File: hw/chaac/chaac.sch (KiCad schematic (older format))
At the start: 58 parts, among them J1 windrain, J2 chaac_radio, J3 chaac_radio, J4 AM2315, J5 Battery, J6 Solar Panel, J7 UART, Q1 Q_PMOS_GSD, SW1 RST, SW2 RST, U1 MIC550X, U2 BMP280, U3 MCP73871

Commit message: Released chaac v3.1 to OSHPark
Moved NRF52 back into chaac pcb.
Removed external T/H connector, switched to BME280 for temp, humidity,
and pressure sensing.

Using RP-SMA connector for this version.
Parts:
- removed J2, J3: chaac_radio, alvarop:20021121-00016C4LF, symbol Connector_Generic:Conn_02x08_Odd_Even
- removed J4: AM2315, TerminalBlock_TE-Connectivity:TerminalBlock_TE_282834-4_1x04_P2.54mm_Horizontal, symbol Connector_Generic:Conn_01x04
- removed U2: BMP280, alvarop:BMP280, symbol alvarop:BMP280
- added C10, C17, C9: 0.1uF, Capacitor_SMD:C_0402_1005Metric, symbol Device:C_Small
- added C11, C12, C13, C15: 12pF, Capacitor_SMD:C_0402_1005Metric, symbol Device:C_Small
- added C14: 100pF, Capacitor_SMD:C_0402_1005Metric, symbol Device:C_Small
- added C16: DNP, Capacitor_SMD:C_0402_1005Metric, symbol Device:C_Small
- added C7: 1uF, Capacitor_SMD:C_0402_1005Metric, symbol Device:C_Small
- added C8: 4.7uF, Capacitor_SMD:C_0402_1005Metric, symbol Device:C_Small
- added F1: 2450FM07A0029T, alvarop:2450FM07A0029T, symbol alvarop:2450FM07A0029T
- added J3: Conn_Coaxial, Connector_Coaxial:SMA_Samtec_SMA-J-P-H-ST-EM1_EdgeMount, symbol Connector:Conn_Coaxial
- added J4: TC2030-CTX, alvarop:TC2030-NL, symbol alvarop:TC2030-CTX
- added L1: 15nH, Inductor_SMD:L_0402_1005Metric, symbol Device:L_Small
- added L2: 10uH, Inductor_SMD:L_0603_1608Metric, symbol Device:L_Small
- added U3: NRF52811-QFAA, alvarop:NRF52811-QFN48, symbol alvarop:NRF52811-QFAA
- added U4: BME280, alvarop:BME280, symbol alvarop:BME280
- added Y1: 32MHz, Crystal:Crystal_SMD_2016-4Pin_2.0x1.6mm, symbol Device:Crystal_GND24
- added Y2: 32.768kHz, Crystal:Crystal_SMD_3215-2Pin_3.2x1.5mm, symbol Device:Crystal_Small
- R3: renamed from R19; value 2k -> 33k; DKPN CR0603-FX-2001ELFCT-ND -> 311-33.0KHRCT-ND; MPN CR0603-FX-2001ELF -> RC0603FR-0733KL
- renumbered C11 to C1, C8 to C18, C2 to C19, C12 to C2, C4 to C20, C7 to C21, C10 to C22, C5 to C23, C3 to C24, C9 to C25, C1 to C3, C6 to C4, C14 to C5, C13 to C6, D3 to D1, D4 to D2, D5 to D3, D6 to D4, D1 to D5, D2 to D6, J6 to J1, J5 to J2, J1 to J5, J7 to J6, R21 to R1, R9 to R10, R12 to R11, R10 to R12, R1 to R14, R2 to R15, R3 to R18, R4 to R19, R22 to R2, R11 to R20, R7 to R21, R14 to R22, R15 to R23, R5 to R24, R6 to R25, R20 to R4, R23 to R5, R18 to R6, R24 to R7, R25 to R8, R8 to R9, U3 to U2
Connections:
- net labels added: ANT, RF_OUT, SWDCLK, SWDIO
- wire segments 243 -> 323
- no-connect marks 23 -> 24
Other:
- note added: "1000V/(33k)=30mA"
- note removed: "1000V/(2k)=500mA"
- note removed: "7-bit I2C Addr: 0x5C"
- moved on the sheet: C1, C18, C19, C2, C20, C21, C22, C23, C24, C25, C3, C4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

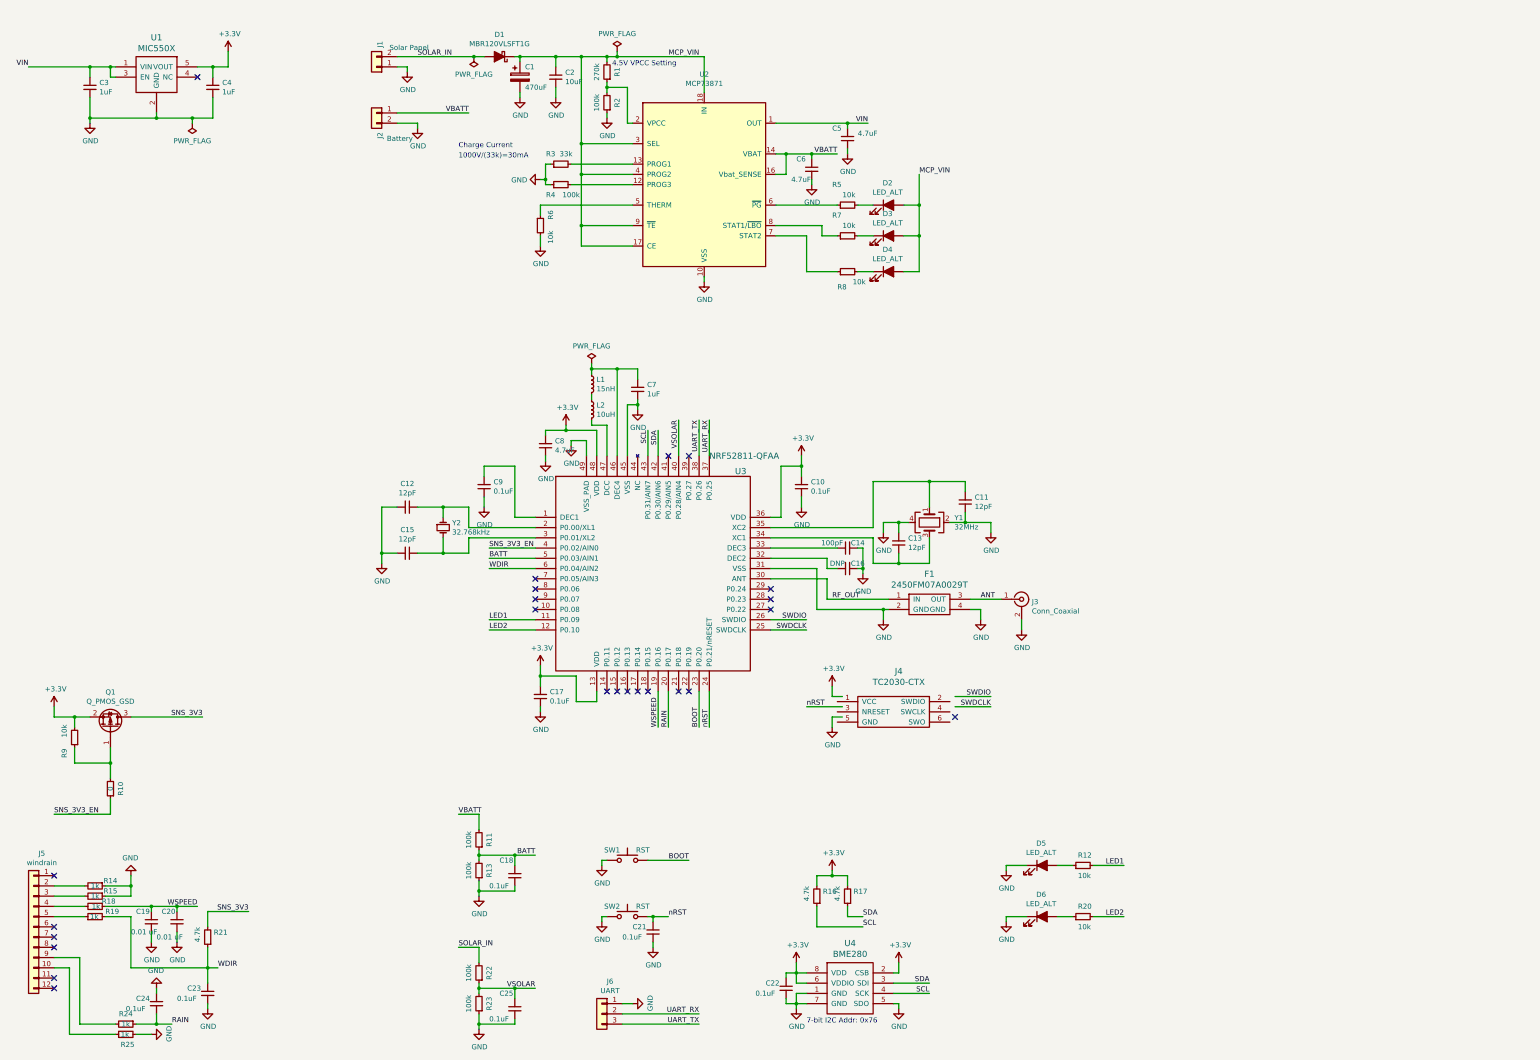
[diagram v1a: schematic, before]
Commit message: Started chaac v4.0 Schematic + layout
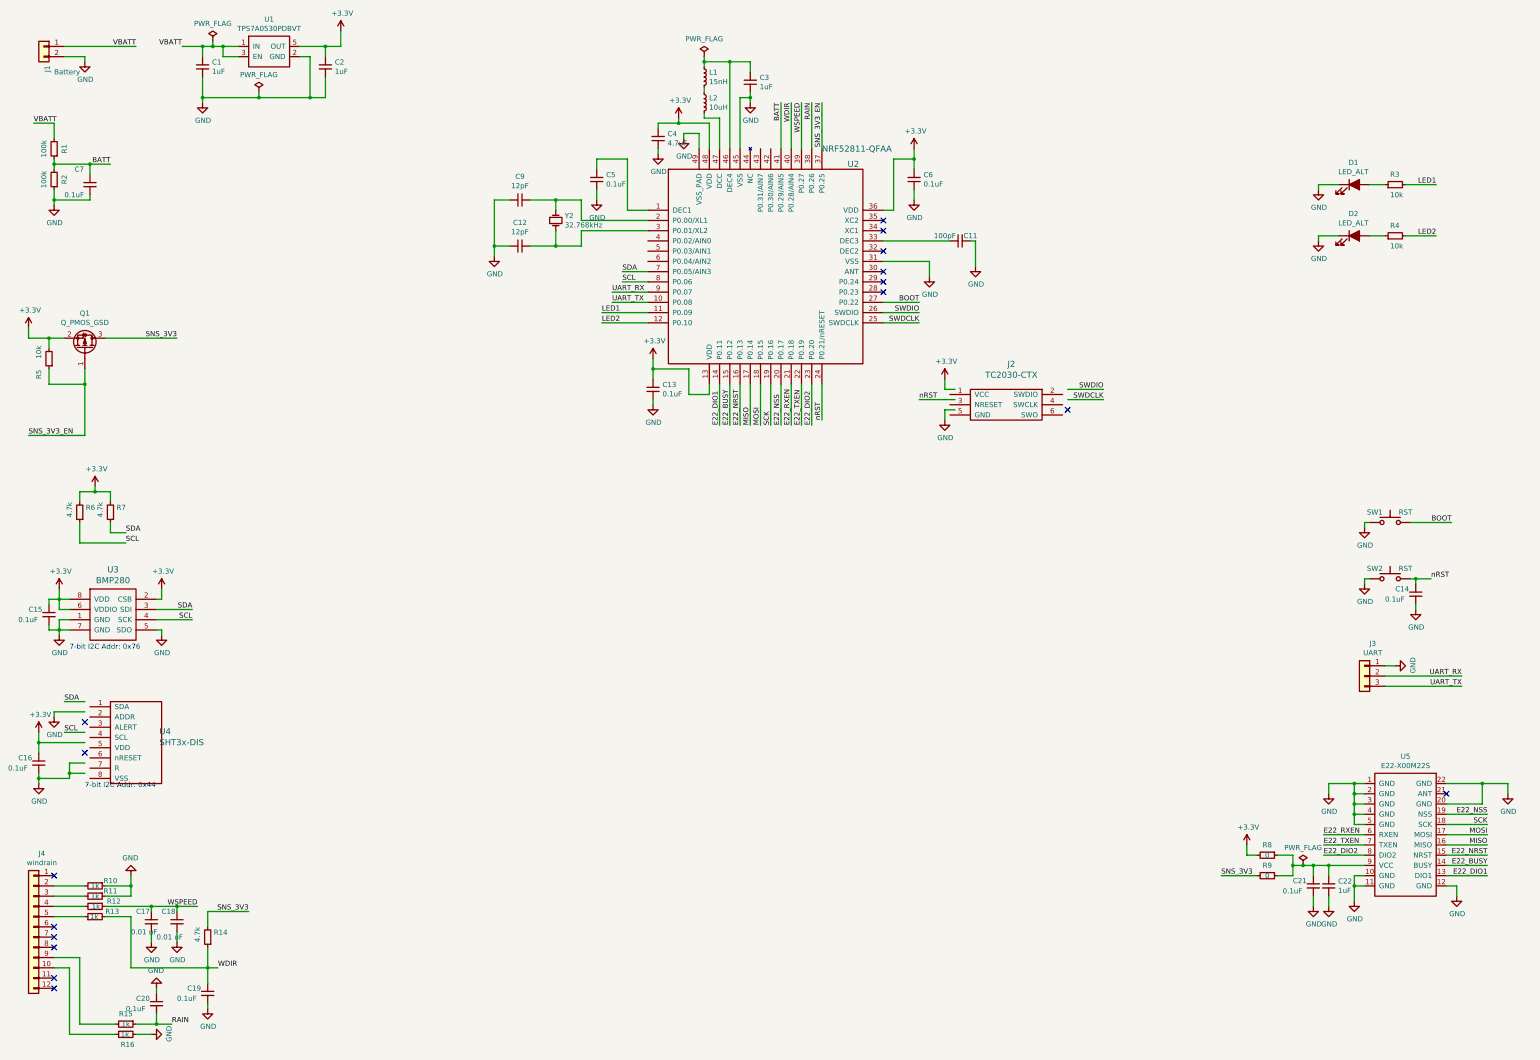
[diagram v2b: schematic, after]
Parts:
- removed C1: 470uF, Capacitor_SMD:CP_Elec_8x10, symbol Device:CP
- removed C11, C13: 12pF, Capacitor_SMD:C_0402_1005Metric, symbol Device:C_Small
- removed C2: 10uF, Capacitor_SMD:C_0805_2012Metric, symbol Device:C_Small
- removed C25: 0.1uF, Capacitor_SMD:C_0603_1608Metric, symbol Device:C_Small
- removed C5, C6: 4.7uF, Capacitor_SMD:C_0603_1608Metric, symbol Device:C_Small
- removed D1: MBR120VLSFT1G, Diode_SMD:D_SOD-123F, symbol Device:D_Schottky_ALT
- removed D2, D3, D4: LED_ALT, LED_SMD:LED_0603_1608Metric, symbol Device:LED_ALT
- removed F1: 2450FM07A0029T, alvarop:2450FM07A0029T, symbol alvarop:2450FM07A0029T
- removed J1: Solar Panel, TerminalBlock_TE-Connectivity:TerminalBlock_TE_282834-2_1x02_P2.54mm_Horizontal, symbol Connector_Generic:Conn_01x02
- removed J3: Conn_Coaxial, Connector_Coaxial:SMA_Samtec_SMA-J-P-H-ST-EM1_EdgeMount, symbol Connector:Conn_Coaxial
- removed R1: 270k, Resistor_SMD:R_0603_1608Metric, symbol Device:R_Small
- removed R10: 0, Resistor_SMD:R_0603_1608Metric, symbol Device:R_Small
- removed R2, R22, R23, R4: 100k, Resistor_SMD:R_0603_1608Metric, symbol Device:R_Small
- removed R3: 33k, Resistor_SMD:R_0603_1608Metric, symbol Device:R_Small
- removed R5, R6, R7: 10k, Resistor_SMD:R_0603_1608Metric, symbol Device:R_Small
- removed U1: MIC550X, alvarop:SOT-23(M5), symbol alvarop:MIC550X
- removed U2: MCP73871, alvarop:MCP73871, symbol Battery_Management:MCP73871
- removed U4: BME280, alvarop:BME280, symbol alvarop:BME280
- removed Y1: 32MHz, Crystal:Crystal_SMD_2016-4Pin_2.0x1.6mm, symbol Device:Crystal_GND24
- added C21: 0.1uF, Capacitor_SMD:C_0603_1608Metric, symbol Device:C_Small
- added C22: 1uF, Capacitor_SMD:C_0603_1608Metric, symbol Device:C_Small
- added R9: 0, Resistor_SMD:R_0603_1608Metric, symbol Device:R_Small
- added U1: TPS7A0530PDBVT, alvarop:SOT-23(M5), symbol alvarop:TPS7A0530PDBVT
- added U3: BMP280, alvarop:BMP280, symbol alvarop:BMP280
- added U4: SHT3x-DIS, alvarop:SHT3x, symbol alvarop:SHT3x-DIS
- added U5: E22-X00M22S, alvarop:E22-X00M22S, symbol alvarop:E22-X00M22S
- C16: value DNP -> 0.1uF; footprint Capacitor_SMD:C_0402_1005Metric -> Capacitor_SMD:C_0603_1608Metric; DKPN (none) -> 490-1532-1-ND; MPN (none) -> GRM188R71C104KA01D
- J1: renamed from J2; footprint alvarop:S2B-PH-SM4-TB -> alvarop:‎282837-2‎
- R8: value 10k -> 0; DKPN 311-10.0KHRCT-ND -> (none); MPN RC0603FR-0710KL -> (none)
- renumbered C3 to C1, C14 to C11, C15 to C12, C17 to C13, C21 to C14, C22 to C15, C19 to C17, C20 to C18, C23 to C19, C4 to C2, C24 to C20, C7 to C3, C8 to C4, C9 to C5, C10 to C6, C18 to C7, C12 to C9, D5 to D1, D6 to D2, J4 to J2, J6 to J3, J5 to J4, R11 to R1, R14 to R10, R15 to R11, R18 to R12, R19 to R13, R21 to R14, R24 to R15, R25 to R16, R13 to R2, R12 to R3, R20 to R4, R9 to R5, R16 to R6, R17 to R7, U3 to U2
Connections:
- net labels added: E22_BUSY, E22_DIO1, E22_DIO2, E22_NRST, E22_NSS, E22_RXEN, E22_TXEN, MISO, MOSI, SCK
- net labels removed: ANT, MCP_VIN, RF_OUT, SOLAR_IN, VIN, VSOLAR
- wire segments 323 -> 280
- no-connect marks 24 -> 16
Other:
- note added: "7-bit I2C Addr: 0x44"
- note removed: "1000V/(33k)=30mA"
- note removed: "4.5V VPCC Setting"
- note removed: "Charge Current"
- moved on the sheet: C1, C11, C12, C13, C14, C15, C2, C3, C4, C5, C6, C7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

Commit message: Finished chaac v4.0!
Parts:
- J1: footprint alvarop:‎282837-2‎ -> TerminalBlock_TE-Connectivity:TerminalBlock_TE_282834-2_1x02_P2.54mm_Horizontal
- U2: footprint alvarop:NRF52811-QFN48 -> alvarop:NRF52811-QFN48-VIAS
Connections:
- no-connect marks 16 -> 21
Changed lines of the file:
@@
 Sheet 1 1
 Title "Chaac"
-Date "2020-06-15"
+Date "2020-06-16"
 Rev "4.0"
 Comp "@alvaroprieto"
@@
 L Connector_Generic:Conn_01x02 J1
 U 1 1 5D0543CF
-P 1350 1100
-F 0 "J1" V 1316 912 50  0000 R CNN
-F 1 "Battery" H 1250 850 50  0000 R CNN
-F 2 "alvarop:‎282837-2‎" H 1350 1100 50  0001 C CNN
-F 3 "~" H 1350 1100 50  0001 C CNN
-F 4 "S2B-PH-SM4-TB(LF)(SN)" V 1350 1100 50  0001 C CNN "MPN"
-F 5 "455-1749-1-ND" V 1350 1100 50  0001 C CNN "DKPN"
-	1    1350 1100
-	-1   0    0    -1
+P 1350 1200
+F 0 "J1" V 1316 1012 50  0000 R CNN
+F 1 "Battery" H 1250 950 50  0000 R CNN
+F 2 "TerminalBlock_TE-Connectivity:TerminalBlock_TE_282834-2_1x02_P2.54mm_Horizontal" H 1350 1200 50  0001 C CNN
+F 3 "~" H 1350 1200 50  0001 C CNN
+F 4 "S2B-PH-SM4-TB(LF)(SN)" V 1350 1200 50  0001 C CNN "MPN"
+F 5 "455-1749-1-ND" V 1350 1200 50  0001 C CNN "DKPN"
+	1    1350 1200
+	-1   0    0    1
 $EndComp
 Wire Wire Line
@@
 U 1 1 5D925286
 P 7350 2000
-F 0 "C4" H 7258 1954 50  0000 R CNN
-F 1 "4.7uF" H 7258 2045 50  0000 R CNN
+F 0 "C4" H 7550 1950 50  0000 R CNN
+F 1 "4.7uF" H 7600 2100 50  0000 R CNN
 F 2 "Capacitor_SMD:C_0402_1005Metric" H 7350 2000 50  0001 C CNN
 F 3 "~" H 7350 2000 50  0001 C CNN
@@
 Connection ~ 7800 1250
 Wire Wire Line
-	7250 3700 6800 3700
-Text Label 6800 3700 0    50   ~ 0
+	7250 3300 6800 3300
+Text Label 6800 3400 0    50   ~ 0
 LED1
 Wire Wire Line
-	7250 3800 6800 3800
-Text Label 6800 3800 0    50   ~ 0
+	7250 3400 6800 3400
+Text Label 6800 3300 0    50   ~ 0
 LED2
 Wire Wire Line
 	7250 3500 6900 3500
-Text Label 6900 3500 0    50   ~ 0
+Text Label 6900 3700 0    50   ~ 0
 UART_RX
-Text Label 6900 3600 0    50   ~ 0
+Text Label 6900 3800 0    50   ~ 0
 UART_TX
 Wire Wire Line
@@
 F 0 "U2" H 9200 4250 60  0000 L CNN
 F 1 "NRF52811-QFAA" H 8950 4400 60  0000 L CNN
-F 2 "alvarop:NRF52811-QFN48" H 7250 3800 50  0001 C CNN
+F 2 "alvarop:NRF52811-QFN48-VIAS" H 7250 3800 50  0001 C CNN
 F 3 "" H 7250 3800 50  0001 C CNN
 F 4 "‎1490-1075-1-ND‎" H 8400 3250 50  0001 C CNN "DKPN"
@@
 	1    0    0    -1
 $EndComp
-Wire Wire Line
-	8150 4800 8150 4400
-Wire Wire Line
-	8050 4800 8050 4400
-Wire Wire Line
-	7950 4800 7950 4400
-Wire Wire Line
-	8450 4800 8450 4400
-Wire Wire Line
-	8350 4800 8350 4400
-Wire Wire Line
-	8250 4800 8250 4400
-Wire Wire Line
-	8550 4400 8550 4800
-Text Label 8550 4800 1    50   ~ 0
-E22_NSS
-Text Label 8450 4800 1    50   ~ 0
-SCK
-Text Label 8350 4800 1    50   ~ 0
-MOSI
-Text Label 8250 4800 1    50   ~ 0
-MISO
-Text Label 8150 4800 1    50   ~ 0
-E22_NRST
-Text Label 8050 4800 1    50   ~ 0
-E22_BUSY
-Text Label 7950 4800 1    50   ~ 0
-E22_DIO1
-Wire Wire Line
-	8650 4400 8650 4800
-Wire Wire Line
-	8750 4400 8750 4800
-Wire Wire Line
-	8850 4400 8850 4800
-Text Label 8650 4800 1    50   ~ 0
-E22_RXEN
-Text Label 8750 4800 1    50   ~ 0
-E22_TXEN
-Text Label 8850 4800 1    50   ~ 0
-E22_DIO2
 $Comp
 L Device:R_Small R8
@@
 Wire Wire Line
 	7250 2800 6600 2800
-Text Label 8650 1650 3    50   ~ 0
+Text Label 8450 1750 3    50   ~ 0
 WDIR
 Wire Wire Line
-	8650 2100 8650 1650
+	8650 2100 8650 1750
 Text Label 8950 1650 3    50   ~ 0
 SNS_3V3_EN
 Wire Wire Line
 	8950 2100 8950 1650
-Text Label 8850 1650 3    50   ~ 0
+Text Label 8350 1850 3    50   ~ 0
 RAIN
 Wire Wire Line
-	8850 2100 8850 1650
-Text Label 8750 1650 3    50   ~ 0
+	8550 2100 8550 1750
+Text Label 8550 1750 3    50   ~ 0
 WSPEED
 Wire Wire Line
-	8750 2100 8750 1650
-Text Label 8550 1650 3    50   ~ 0
+	8450 2100 8450 1750
+Text Label 8650 1750 3    50   ~ 0
 BATT
 Wire Wire Line
-	8550 2100 8550 1650
-Text Label 7000 3300 0    50   ~ 0
+	8350 2100 8350 1850
+Text Label 6900 3500 0    50   ~ 0
 SDA
 Wire Wire Line
-	7250 3300 7000 3300
-Text Label 7000 3400 0    50   ~ 0
+	7250 3700 6900 3700
+Text Label 6900 3600 0    50   ~ 0
 SCL
 Wire Wire Line
-	7250 3400 7000 3400
+	7250 3800 6900 3800
+Text Label 7950 4800 1    50   ~ 0
+E22_DIO1
+Text Label 8050 4800 1    50   ~ 0
+E22_BUSY
+Text Label 8150 4800 1    50   ~ 0
+E22_NRST
+Text Label 8250 4800 1    50   ~ 0
+MISO
+Text Label 8350 4800 1    50   ~ 0
+MOSI
+Text Label 8450 4800 1    50   ~ 0
+SCK
+Text Label 8550 4800 1    50   ~ 0
+E22_NSS
+Wire Wire Line
+	8550 4400 8550 4800
+Wire Wire Line
+	8250 4800 8250 4400
+Wire Wire Line
+	8350 4800 8350 4400
+Wire Wire Line
+	8450 4800 8450 4400
+Wire Wire Line
+	7950 4800 7950 4400
+Wire Wire Line
+	8050 4800 8050 4400
+Wire Wire Line
+	8150 4800 8150 4400
+Wire Wire Line
+	8850 4400 8850 4800
+Text Label 8850 4800 1    50   ~ 0
+E22_DIO2
+Text Label 8750 4800 1    50   ~ 0
+E22_TXEN
+Text Label 8650 4800 1    50   ~ 0
+E22_RXEN
+Wire Wire Line
+	8750 4400 8750 4800
+Wire Wire Line
+	8650 4400 8650 4800
+NoConn ~ 7250 3200
+NoConn ~ 7250 3100
+NoConn ~ 7250 3000
+NoConn ~ 8850 2100
+NoConn ~ 8750 2100
 $EndSCHEMATC

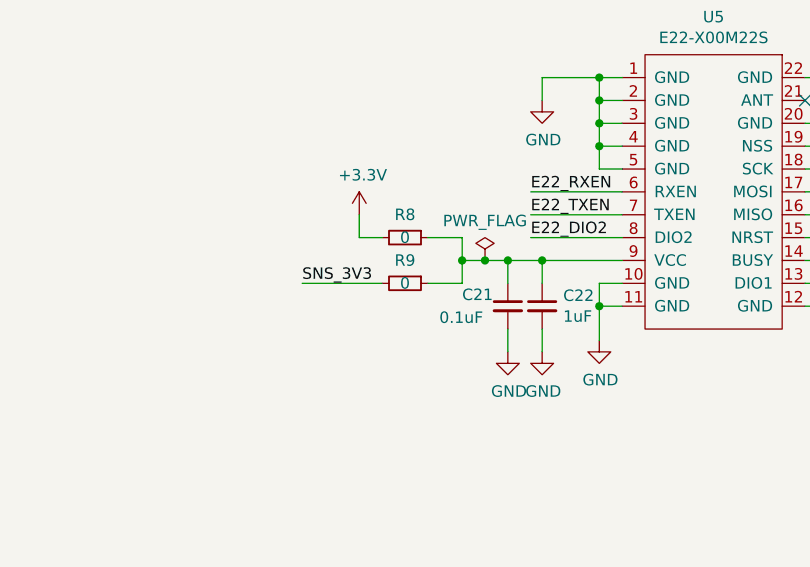
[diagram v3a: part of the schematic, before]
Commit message: Update components for chaac schematic
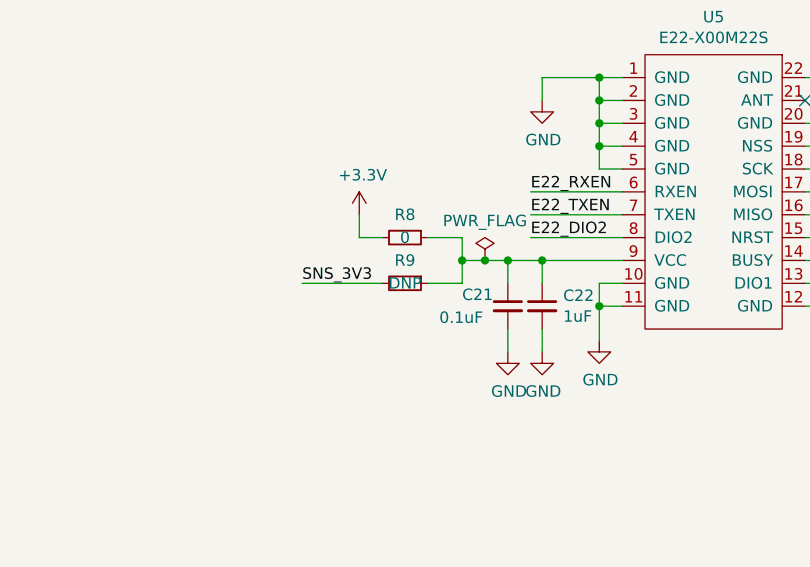
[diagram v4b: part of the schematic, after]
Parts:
- J1: DKPN 455-1749-1-ND -> A98333-ND; MPN S2B-PH-SM4-TB(LF)(SN) -> 282834-2
- R8: DKPN (none) -> 311-0.0GRCT-ND; MPN (none) -> RC0603JR-070RL
- R9: value 0 -> DNP
- U1: DKPN (none) -> 296-50829-1-ND; MPN (none) -> TPS7A0530PDBVT
- U3: DKPN (none) -> 828-1064-1-ND; MPN (none) -> BMP280
- U4: DKPN (none) -> 1649-1066-1-ND; MPN (none) -> SHT31-DIS-F2.5KS
- U5: MPN (none) -> E22-X00M22S
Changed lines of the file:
@@
 F 2 "TerminalBlock_TE-Connectivity:TerminalBlock_TE_282834-2_1x02_P2.54mm_Horizontal" H 1350 1200 50  0001 C CNN
 F 3 "~" H 1350 1200 50  0001 C CNN
-F 4 "S2B-PH-SM4-TB(LF)(SN)" V 1350 1200 50  0001 C CNN "MPN"
-F 5 "455-1749-1-ND" V 1350 1200 50  0001 C CNN "DKPN"
+F 4 "282834-2" V 1350 1200 50  0001 C CNN "MPN"
+F 5 "A98333-ND" V 1350 1200 50  0001 C CNN "DKPN"
 	1    1350 1200
 	-1   0    0    1
@@
 F 2 "alvarop:BMP280" H 1600 6800 50  0001 C CNN
 F 3 "" H 1600 6800 50  0001 C CNN
+F 4 "828-1064-1-ND" H 2050 6650 50  0001 C CNN "DKPN"
+F 5 "BMP280" H 2050 6650 50  0001 C CNN "MPN"
 	1    2050 6650
 	1    0    0    -1
@@
 F 2 "alvarop:SHT3x" H 1950 7850 60  0001 C CNN
 F 3 "" H 1950 7850 60  0000 C CNN
+F 4 "1649-1066-1-ND" H 2200 7850 50  0001 C CNN "DKPN"
+F 5 "SHT31-DIS-F2.5KS" H 2200 7850 50  0001 C CNN "MPN"
 	1    2200 7850
 	1    0    0    -1
@@
 F 2 "alvarop:E22-X00M22S" H 14650 8800 50  0001 C CNN
 F 3 "" H 14650 8800 50  0001 C CNN
+F 4 "E22-X00M22S" H 14650 8800 50  0001 C CNN "MPN"
 	1    14650 8800
 	1    0    0    -1
@@
 F 2 "alvarop:SOT-23(M5)" H 3650 1300 50  0001 C CNN
 F 3 "https://www.ti.com/lit/ds/symlink/tps7a05.pdf?HQS=TI-null-null-digikeymode-df-pf-null-wwe&ts=1592235148763" H 3650 1300 50  0001 C CNN
+F 4 "296-50829-1-ND" H 3550 1300 50  0001 C CNN "DKPN"
+F 5 "TPS7A0530PDBVT" H 3550 1300 50  0001 C CNN "MPN"
 	1    3550 1300
 	1    0    0    -1
@@
 F 2 "Resistor_SMD:R_0603_1608Metric" H 13300 9000 50  0001 C CNN
 F 3 "~" H 13300 9000 50  0001 C CNN
+F 4 "311-0.0GRCT-ND" H 13300 9000 50  0001 C CNN "DKPN"
+F 5 "RC0603JR-070RL" H 13300 9000 50  0001 C CNN "MPN"
 	1    13300 9000
 	0    1    1    0
@@
 P 13300 9200
 F 0 "R9" V 13200 9200 50  0000 C CNN
-F 1 "0" V 13300 9200 50  0000 C CNN
+F 1 "DNP" V 13300 9200 50  0000 C CNN
 F 2 "Resistor_SMD:R_0603_1608Metric" H 13300 9200 50  0001 C CNN
 F 3 "~" H 13300 9200 50  0001 C CNN
